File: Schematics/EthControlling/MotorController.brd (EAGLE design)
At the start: 90 x 80 mm, 109 parts, among them IC1 TLP621-2, IC2 MEGA164P/324P/644P-AU, IC3 OPA4234P, IC4 TLP621-2, Q1 20.000M, T1 2SC1815, T2 2SC1815, T3 2SC1815, T4 2SC1815

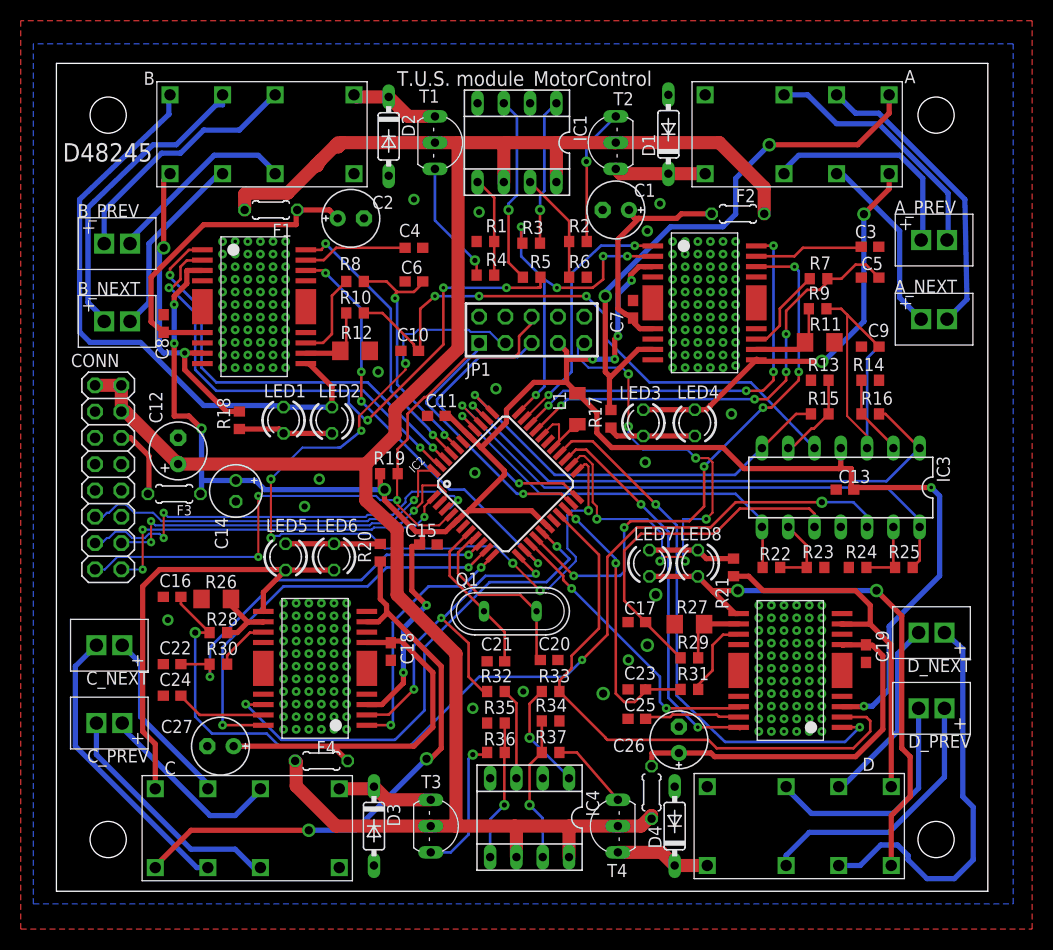
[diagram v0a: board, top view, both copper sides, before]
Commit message: fix wiring of MotorController.sch and clear DRC errors
Signed-off-by: sosoru <siva6991@yahoo.co.jp>
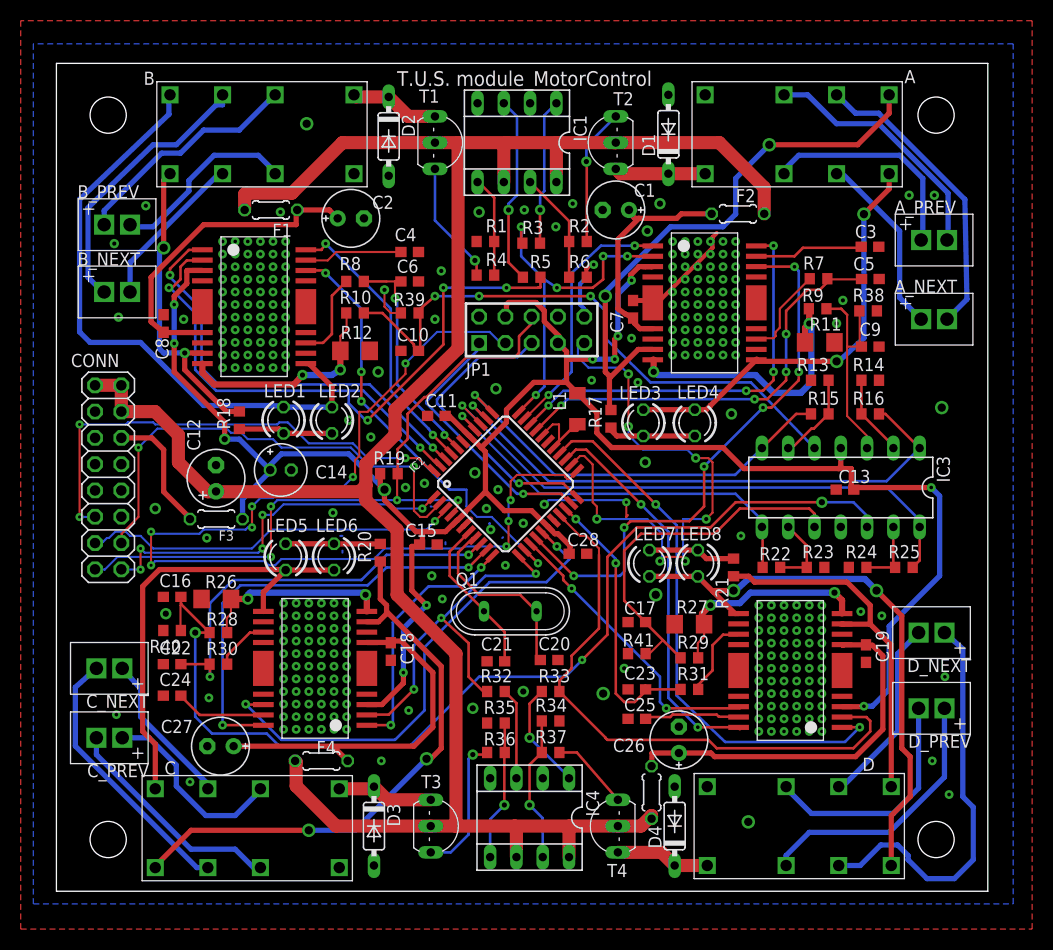
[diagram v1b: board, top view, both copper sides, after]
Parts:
- added C28: 0.1u, rcl:C0603
- added R38, R39, R40, R41: 1Meg, resistor:R0603
- C10, C16, C17, C9: value 0.47u -> 4.7u
- R10, R28, R29, R9: value 33k -> 3.3k
- R11, R12, R26, R27: value 0.01 -> 0.1
- R13, R14, R23, R24: value 100 -> 1k
- moved C14 4.79 mm to (21.7, 40.7), turned to 0 degrees
- moved F3 4.74 mm to (15.4, 36.0)
- moved C12 4.51 mm to (15.4, 39.9)
- moved B_NEXT 2.84 mm to (7.11, 57.9)
- moved C_NEXT 2.24 mm to (3.86, 21.5)
- moved B_PREV 1.83 mm to (7.11, 64.4)
- moved C_PREV 1.42 mm to (3.86, 14.8)
- moved C4 0.57 mm to (34.1, 61.8)
- moved C6 0.41 mm to (34.1, 58.9), turned to 0 degrees
- moved C5 0.14 mm to (78.7, 59.2), turned to 0 degrees
- turned C9 to 0 degrees
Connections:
- net +5V: now also C28.2, JP1.4
- net GND: now also C28.1, R38.2, R39.2, R40.2, R41.2, U$1.10, U$2.10, U$3.10, U$4.10; no longer U$1.8, U$2.8, U$3.8, U$4.8
- net N$14: now also U$1.8; no longer U$1.10
- net N$21: now also R38.1
- net N$30: now also R40.1
- net N$31: now also U$3.8; no longer U$3.10
- net N$45: now also R39.1
- net N$46: now also U$2.8; no longer U$2.10
- net N$60: now also R41.1
- net N$61: now also U$4.8; no longer U$4.10
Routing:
- net GND: track 1.26 -> 36.2 mm, vias 282 -> 321
- net N$14: track 8.40 -> 27.0 mm, vias 0 -> 2
- net TDO: track 84.3 -> 100.6 mm, vias 7 -> 9
- net N$61: track 6.83 -> 20.6 mm, vias 0 -> 2
- net N$46: track 7.32 -> 21.0 mm, vias 0 -> 2
- net N$31: track 6.84 -> 18.7 mm, vias 0 -> 2
- net +5V: track 203.8 -> 215.5 mm
- net N$21: track 30.6 -> 20.9 mm
- net !SS: track 37.4 -> 47.1 mm, vias 1 -> 3
- net MISO: track 37.7 -> 46.4 mm, vias 3 -> 2
- net SCK: track 43.0 -> 36.7 mm, vias 3 -> 1
- net N$54: track 7.15 -> 12.5 mm
- net N$37: track 18.2 -> 15.3 mm
- net CTRL_A_ALERT: track 44.4 -> 41.6 mm
- net N$30: track 96.6 -> 99.2 mm
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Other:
- board text removed: "D48245"

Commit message: renumber MotorController.brd
Signed-off-by: sosoru <siva6991@yahoo.co.jp>
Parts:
- C10, C16, C6: value 4.7u -> 0.1u
- C11, C18, C24, C8: value 0.1u -> 4.7u
- C13: value 0.1u -> 100u; device rcl:C0603 -> rcl:E2-5
- C14: value 100u -> 0.1u; device rcl:E2-5 -> rcl:C0603
- C20: value 22p -> 0.1u
- C22: value 4.7u -> 22p
- C27: value (none) -> 0.1u; device rcl:E2,5-6E -> rcl:C0603
- C28: value 0.1u -> (none); device rcl:C0603 -> rcl:E2,5-6E
- R1: value 100k -> 3.3k
- R11: value 0.1 -> 3.3k; device resistor:R1206 -> resistor:R0603
- R13: value 1k -> 1Meg
- R14, R23: value 1k -> 3.3k
- R15: value 25k -> 0.1; device resistor:R0603 -> resistor:R1206
- R16: value 25k -> 3.3k
- R17: value 3.3k -> 1k
- R18, R20: value 3.3k -> 25k
- R19: value 10k -> 1k
- R2, R36, R37: value 10k -> 3.3k
- R22: value 25k -> 10k
- R24: value 1k -> 25k
- R25: value 25k -> 1k
- R26: value 0.1 -> 1k; device resistor:R1206 -> resistor:R0603
- R27: value 0.1 -> 25k; device resistor:R1206 -> resistor:R0603
- R28: value 3.3k -> 1Meg
- R29: value 3.3k -> 0.1; device resistor:R0603 -> resistor:R1206
- R3: value 500 -> 1Meg
- R34: value 100k -> 1Meg
- R35: value 100k -> 0.1; device resistor:R0603 -> resistor:R1206
- R38, R40: value 1Meg -> 100k
- R39, R41: value 1Meg -> 10k
- R4: value 10k -> 100k
- R5: value 500 -> 10k
- R6: value 100k -> 500
- R7: value 3.3k -> 500
- R8: value 3.3k -> 10k
- R9: value 3.3k -> 100k
- moved C3 68.7 mm to (10.4, 54.9), turned to 270 degrees
- moved C8 68.4 mm to (78.7, 59.2), turned to 0 degrees
- moved C19 67.2 mm to (11.2, 18.9), turned to 180 degrees
- moved C16 65.8 mm to (76.2, 38.8), turned to 0 degrees
- moved R26 62.1 mm to (77.4, 31.3)
- moved R14 61.1 mm to (17.7, 45.5), turned to 90 degrees
- moved R18 56.1 mm to (73.8, 46.1), turned to 180 degrees
- moved C13 54.6 mm to (21.7, 40.7)
- moved R38 53.7 mm to (42.5, 16.3), turned to 180 degrees
- moved R20 49.2 mm to (78.6, 46.1), turned to 0 degrees
- moved R19 47.4 mm to (78.6, 49.4)
- moved R29 46.1 mm to (15.4, 28.2)
- moved R31 45.6 mm to (15.6, 21.9)
- moved R15 45.3 mm to (28.9, 52.2), turned to 0 degrees
- moved C17 45.0 mm to (11.2, 28.4)
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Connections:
- removed net N$14 (its old number): R11.1, R9.1, U$1.8
- new net N$46: R15.1, R2.1, U$1.8
- net !RESET: now also R22.2; no longer R19.2
- net +5V: now also C10.2, C13.+, C14.2, C16.2, R22.1; no longer C11.2, C13.2, C14.+, C28.2, R19.1
- net A_OUT1: now also R16.2, U$2.7; no longer R17.2, U$1.7
- net A_OUT2: now also U$2.9; no longer U$1.9
- net A_OUT3: now also R21.2; no longer R20.2
- net A_OUT5: now also R14.2, U$1.7; no longer R18.2, U$2.7
- net A_OUT6: now also U$1.9; no longer U$2.9
- net A_OUT7: now also R23.2; no longer R21.2
- net CTRL_A_1: now also U$2.1; no longer U$1.1
- net CTRL_A_2: now also U$2.16; no longer U$1.16
- net CTRL_A_3: now also R6.1, U$2.2; no longer R3.1, U$1.2
- net CTRL_A_ALERT: now also C8.1, R11.2; no longer C5.1, R7.2
- net CTRL_A_PWM: now also U$2.14; no longer U$1.14
- net CTRL_B_1: now also U$1.1; no longer U$2.1
- net CTRL_B_2: now also U$1.16; no longer U$2.16
- net CTRL_B_3: now also R7.1, U$1.2; no longer R5.1, U$2.2
- net CTRL_B_ALERT: now also C5.1, R1.2; no longer C6.1, R8.2
- net CTRL_B_PWM: now also U$1.14; no longer U$2.14
- net CTRL_C_ALERT: now also C18.1, R31.2; no longer C22.1, R30.2
- net CTRL_D_ALERT: now also C24.1, R37.2; no longer C23.1, R31.2
- net FEEDBACK_A: now also R20.2; no longer R16.2
- net FEEDBACK_B: now also R18.2; no longer R15.2
- net FEEDBACK_C: now also R27.2; no longer R25.2
- net FEEDBACK_D: now also R24.2; no longer R22.2
- net GND: now also C10.1, C11.2, C13.-, C14.1, C16.1, C18.2, C19.2, C22.1, C25.1, C27.2, C28.-, C3.1, C6.1, C7.2, C8.2, R15.2, R17.2, R19.2, R25.2, R28.2, R29.2, R3.2, R4.2, R9.2; no longer C10.2, C11.1, C13.1, C14.-, C16.2, C18.1, C19.1, C22.2, C25.2, C27.-, C28.1, C3.2, C6.2, C7.1, C8.1, R1.2, R11.2, R14.2, R23.2, R24.2, R27.2, R39.2, R41.2, R6.2
- net N$10: now also C2.+, C6.2, U$2.5; no longer C1.+, C7.2, U$1.5
- net N$11: now also R19.1, R20.1; no longer R14.1, R16.1
- net N$12: now also R31.1; no longer R30.1
- net N$18: now also C20.2, C26.+; no longer C18.2, C27.+
- net N$19: now also R21.1; no longer R20.1
- net N$20: now also R7.2; no longer R5.2
- net N$21: now also C11.1, R10.2, R13.1; no longer C9.1, R38.1, R9.2
- net N$26: now also R38.1, R39.1; no longer R35.1, R36.1
- net N$28: now also R39.2; no longer R36.2
- net N$29: now also R26.1, R27.1; no longer R24.1, R25.1
- net N$3: now also C22.2; no longer C20.2
- net N$30: now also C17.1, R28.1, R30.2; no longer C16.1, R28.2, R40.1
- net N$31: now also R29.1, R30.1; no longer R26.1, R28.1
- net N$32: now also U$1.15; no longer U$2.15
- net N$33: now also R1.1, U$1.11; no longer R8.1, U$2.11
- net N$34: now also C1.+, C3.2, U$1.5; no longer C2.+, C8.2, U$2.5
- net N$35: now also R14.1; no longer R18.1
- net N$4: now also R11.1, U$2.11; no longer R7.1, U$1.11
- net N$41: now also R5.1; no longer R1.1
- net N$42: now also D1.C; no longer D2.C
- net N$43: now also R5.2; no longer R4.2
- net N$44: now also R17.1, R18.1; no longer R13.1, R15.1
- net N$45: now also C9.1, R2.2, R3.1; no longer C10.1, R10.2, R39.1
- net N$47: now also C27.1; no longer C25.1
- net N$48: now also R37.1; no longer R31.1
- net N$49: now also C25.2, C28.+; no longer C19.2, C26.+
- net N$5: now also C7.1, U$2.15; no longer C3.1, U$1.15
- net N$50: now also R23.1; no longer R21.1
- net N$56: now also R40.1, R41.1; no longer R34.1, R37.1
- net N$58: now also R41.2; no longer R37.2
- net N$59: now also R24.1, R25.1; no longer R22.1, R23.1
- net N$6: now also R6.2; no longer R3.2
- net N$60: now also C23.1, R34.1, R36.2; no longer C17.1, R29.2, R41.1
- net N$61: now also R35.1, R36.1; no longer R27.1, R29.1
- net N$7: now also R8.1, R9.1; no longer R2.1, R6.1
- net N$8: now also R16.1; no longer R17.1
- net N$84: now also D2.C; no longer D1.C
- net N$86: now also R8.2; no longer R2.2
- net N$9: now also C19.1; no longer C24.1
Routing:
- net N$14 (its old number): track 27.0 -> 0.00 mm, vias 2 -> 0
- net N$46: track 0.00 -> 21.0 mm, vias 0 -> 2
- net N$10: track 23.3 -> 32.0 mm
- net +12V: track 218.9 -> 227.1 mm
- net N$14: track 21.0 -> 27.0 mm
- net CTRL_D_3: track 57.6 -> 58.4 mm
- net GND: vias 321 -> 320
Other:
- board text added: "T.U.S. module_MotorControl Rev.B"
- board text removed: "T.U.S. module_MotorControl"

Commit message: ditto
Signed-off-by: sosoru <siva6991@yahoo.co.jp>
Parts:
- R32, R33, R6, R7: value 500 -> 1k
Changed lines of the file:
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@@
 <attribute name="VALUE" x="55.616" y="44.767" size="1.27" layer="27" font="vector" rot="R90"/>
 </element>
-<element name="R6" library="resistor" package="R0603" value="500" x="45.8768" y="62.8288" smashed="yes">
+<element name="R6" library="resistor" package="R0603" value="1k" x="45.8768" y="62.8288" smashed="yes">
 <attribute name="NAME" x="44.9878" y="63.7178" size="1.27" layer="25" font="vector"/>
 <attribute name="VALUE" x="44.9878" y="60.7968" size="1.27" layer="27" font="vector"/>
@@
 <attribute name="VALUE" x="29.2608" y="33.6042" size="1.27" layer="27" font="vector" rot="R270"/>
 </element>
-<element name="R32" library="resistor" package="R0603" value="500" x="42.4688" y="19.304" smashed="yes">
+<element name="R32" library="resistor" package="R0603" value="1k" x="42.4688" y="19.304" smashed="yes">
 <attribute name="NAME" x="40.9702" y="20.193" size="1.27" layer="25" font="vector"/>
 <attribute name="VALUE" x="41.5798" y="17.272" size="1.27" layer="27" font="vector"/>
@@
 <attribute name="VALUE" x="19.7104" y="44.6278" size="1.27" layer="27" font="vector" rot="R90"/>
 </element>
-<element name="R7" library="resistor" package="R0603" value="500" x="45.9232" y="59.3344" smashed="yes" rot="R180">
+<element name="R7" library="resistor" package="R0603" value="1k" x="45.9232" y="59.3344" smashed="yes" rot="R180">
 <attribute name="NAME" x="47.8282" y="61.4934" size="1.27" layer="25" font="vector" rot="R180"/>
 <attribute name="VALUE" x="46.8122" y="61.3664" size="1.27" layer="27" font="vector" rot="R180"/>
@@
 <attribute name="VALUE" x="63.3984" y="32.1818" size="1.27" layer="27" font="vector" rot="R270"/>
 </element>
-<element name="R33" library="resistor" package="R0603" value="500" x="47.752" y="19.304" smashed="yes" rot="R180">
+<element name="R33" library="resistor" package="R0603" value="1k" x="47.752" y="19.304" smashed="yes" rot="R180">
 <attribute name="NAME" x="49.657" y="21.463" size="1.27" layer="25" font="vector" rot="R180"/>
 <attribute name="VALUE" x="48.641" y="21.336" size="1.27" layer="27" font="vector" rot="R180"/>
